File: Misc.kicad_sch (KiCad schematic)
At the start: 14 parts, among them J501 Conn_01x04, U500 TJA1051T-3

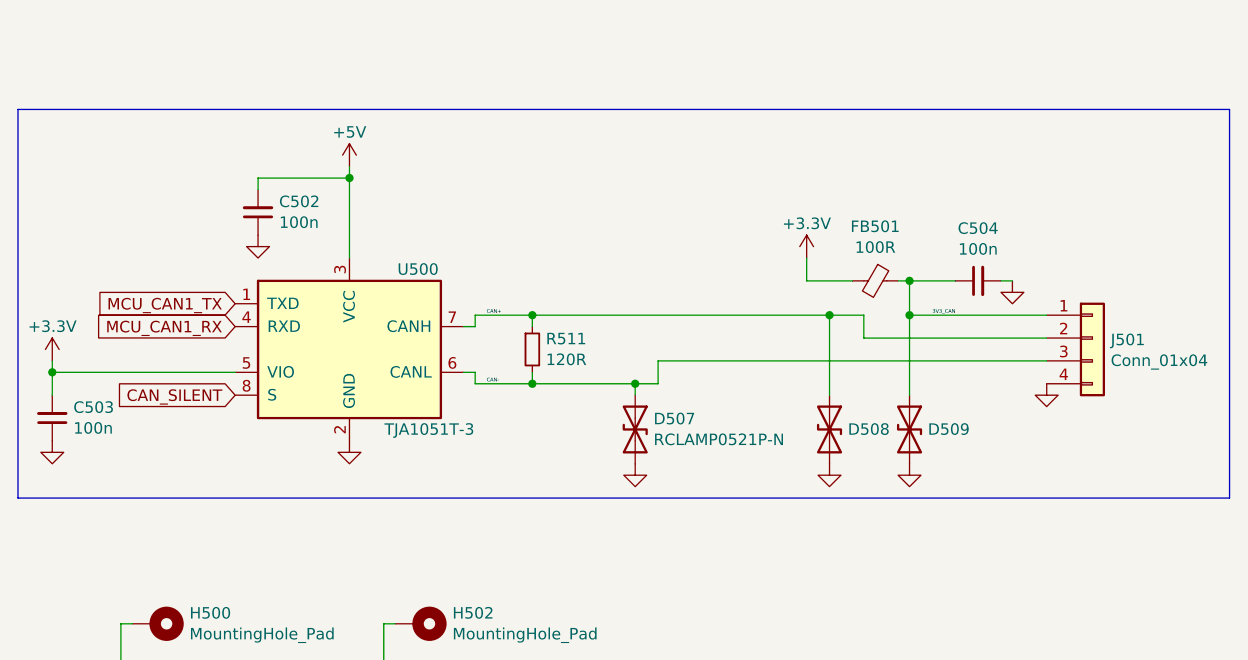
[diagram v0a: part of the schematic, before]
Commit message: replaced CAN transceiver, introduced new IMU
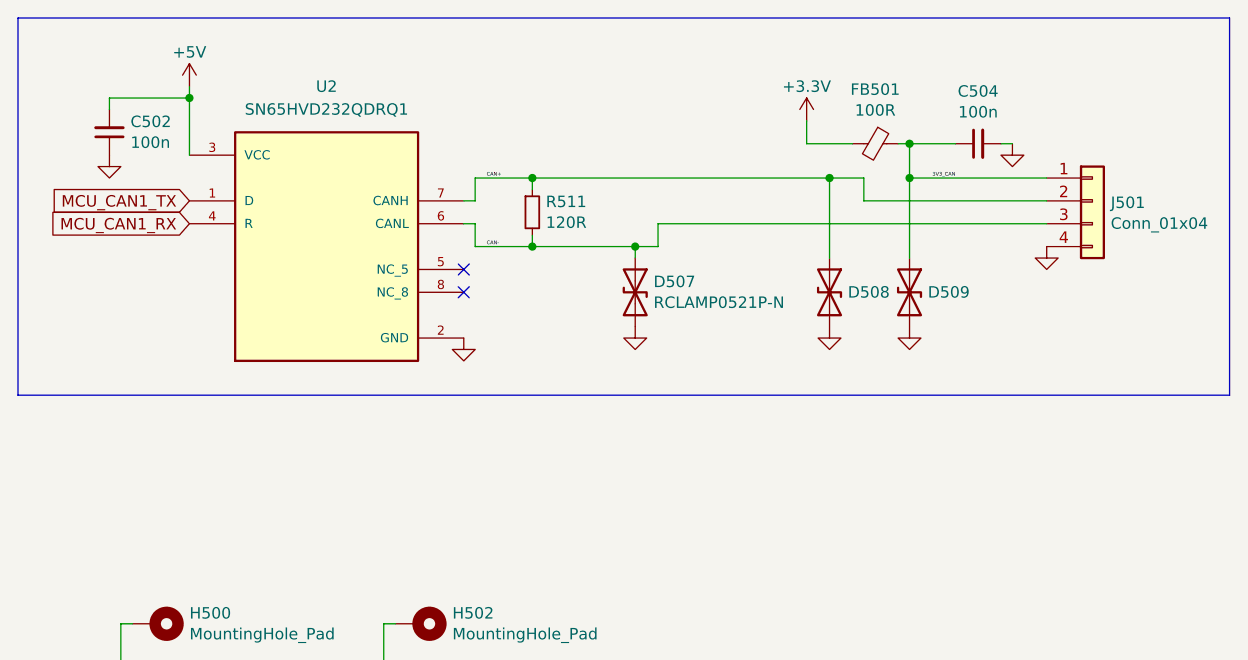
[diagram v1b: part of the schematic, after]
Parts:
- removed C503: 100n, Capacitor_SMD:C_0402_1005Metric, symbol Device:C_Small
- removed U500: TJA1051T-3, Package_SO:SOIC-8_3.9x4.9mm_P1.27mm, symbol Interface_CAN_LIN:TJA1051T-3
- added U2: SN65HVD232QDRQ1, SnapEDA Library:SOIC127P599X175-8N, symbol SN65HVD232QDRQ1:SN65HVD232QDRQ1
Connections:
- net +5V: now also U2.3 (VCC)
- net CAN+: now also U2.7 (CANH)
- net CAN-: now also U2.6 (CANL)
- net GND: now also U2.2 (GND)
- net MCU_CAN1_RX: now also U2.4 (R)
- net MCU_CAN1_TX: now also U2.1 (D)
- no-connect marks 0 -> 2
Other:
- moved on the sheet: C502, C504, D507, D508, D509, FB501, J501, R511

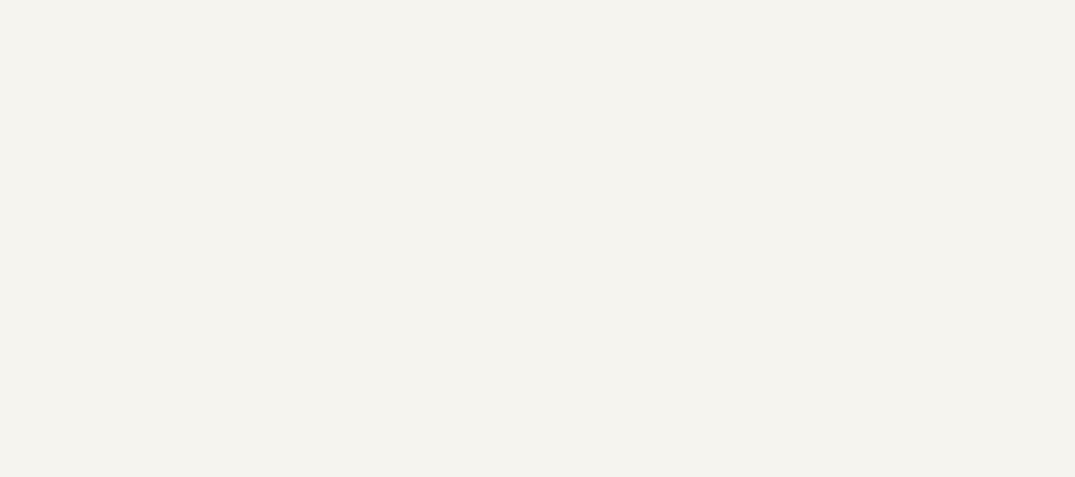
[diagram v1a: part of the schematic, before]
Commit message: added cubeide workspace
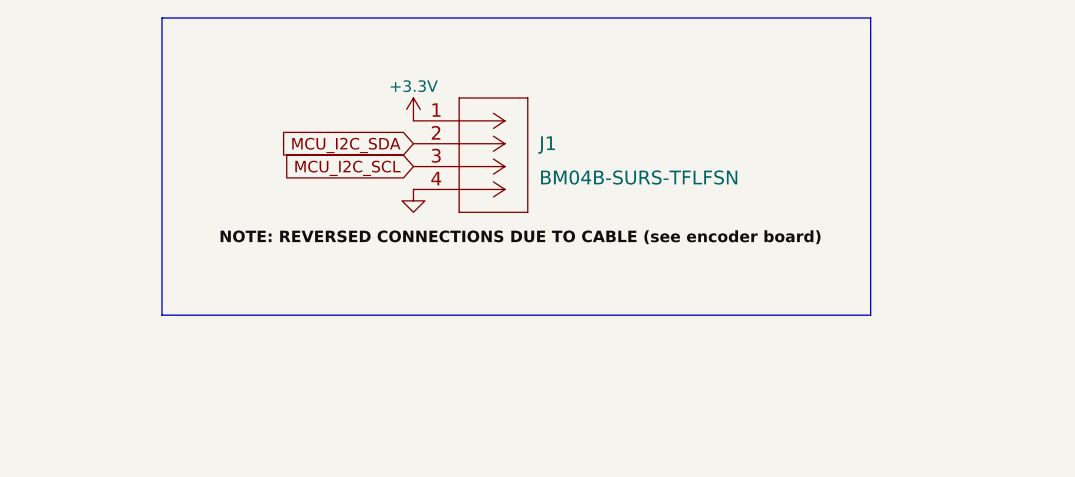
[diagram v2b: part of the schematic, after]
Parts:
- added J1: BM04B-SURS-TFLFSN, CONN_BM04B-SURS-TF_JST, symbol BM04B:BM04B-SURS-TFLFSN
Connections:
- net +3V3: now also J1.1
- net GND: now also J1.4
- new net MCU_I2C_SCL: J1.3
- new net MCU_I2C_SDA: J1.2
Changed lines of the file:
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@@
+    (stroke (width 0) (type default) (color 0 0 0 0))
+  )
+  (polyline (pts (xy 109.22 72.39) (xy 187.96 72.39))
     (stroke (width 0) (type default) (color 0 0 0 0))
   )
@@
     (stroke (width 0) (type default) (color 0 0 0 0))
   )
+  (polyline (pts (xy 109.22 39.37) (xy 109.22 72.39))
+    (stroke (width 0) (type default) (color 0 0 0 0))
+  )
+  (polyline (pts (xy 187.96 72.39) (xy 187.96 39.37))
+    (stroke (width 0) (type default) (color 0 0 0 0))
+  )
   (wire (pts (xy 156.21 127) (xy 156.21 129.54))
     (stroke (width 0) (type default) (color 0 0 0 0))
@@
     (stroke (width 0) (type default) (color 0 0 0 0))
   )
+  (polyline (pts (xy 187.96 39.37) (xy 109.22 39.37))
+    (stroke (width 0) (type default) (color 0 0 0 0))
+  )
   (wire (pts (xy 184.15 121.92) (xy 199.39 121.92))
     (stroke (width 0) (type default) (color 0 0 0 0))
@@
   (wire (pts (xy 104.14 113.03) (xy 95.25 113.03))
     (stroke (width 0) (type default) (color 0 0 0 0))
+  )
+  (label "NOTE: REVERSED CONNECTIONS DUE TO CABLE (see encoder board)"
+    (at 115.57 64.77 0)
+    (effects (font (size 1.27 1.27) (thickness 0.254) bold) (justify left bottom))
   )
   (label "CAN+" (at 137.16 121.92 0)
@@
     )
   )
+  (global_label "MCU_I2C_SCL" (shape input) (at 137.16 55.88 180) (fields_autoplaced)
+    (effects (font (size 1.27 1.27)) (justify right))
+    (property "Intersheet References" "${INTERSHEET_REFS}" (id 0) (at 122.2568 55.8006 0)
+      (effects (font (size 1.27 1.27)) (justify right) hide)
+    )
+  )
   (global_label "MCU_CAN1_TX" (shape input) (at 104.14 124.46 180) (fields_autoplaced)
     (effects (font (size 1.27 1.27)) (justify right))
@@
     )
   )
+  (global_label "MCU_I2C_SDA" (shape input) (at 137.16 53.34 180) (fields_autoplaced)
+    (effects (font (size 1.27 1.27)) (justify right))
+    (property "Intersheet References" "${INTERSHEET_REFS}" (id 0) (at 122.1963 53.2606 0)
+      (effects (font (size 1.27 1.27)) (justify right) hide)
+    )
+  )
   (symbol (lib_id "power:GND") (at 134.62 139.7 0) (unit 1)
     (in_bom yes) (on_board yes)
@@
     (pin "1")
     (pin "2")
+  )
+  (symbol (lib_id "BluePhil-rescue:+3.3V-power") (at 137.16 50.8 0) (unit 1)
+    (in_bom yes) (on_board yes)
+    (property "Reference" "#PWR032" (id 0) (at 137.16 54.61 0)
+      (effects (font (size 1.27 1.27)) hide)
+    )
+    (property "Value" "+3.3V" (id 1) (at 137.16 46.99 0))
+    (property "Footprint" "" (id 2) (at 137.16 50.8 0)
+      (effects (font (size 1.27 1.27)) hide)
+    )
+    (property "Datasheet" "" (id 3) (at 137.16 50.8 0)
+      (effects (font (size 1.27 1.27)) hide)
+    )
+    (pin "1")
   )
   (symbol (lib_id "SN65HVD232QDRQ1:SN65HVD232QDRQ1") (at 119.38 129.54 0) (unit 1)
@@
     (pin "8")
   )
+  (symbol (lib_id "BM04B:BM04B-SURS-TFLFSN") (at 137.16 50.8 0) (unit 1)
+    (in_bom yes) (on_board yes) (fields_autoplaced)
+    (property "Reference" "J1" (id 0) (at 151.13 53.34 0)
+      (effects (font (size 1.524 1.524)) (justify left))
+    )
+    (property "Value" "BM04B-SURS-TFLFSN" (id 1) (at 151.13 57.15 0)
+      (effects (font (size 1.524 1.524)) (justify left))
+    )
+    (property "Footprint" "CONN_BM04B-SURS-TF_JST" (id 2) (at 147.32 57.404 0)
+      (effects (font (size 1.524 1.524)) hide)
+    )
+    (property "Datasheet" "" (id 3) (at 137.16 50.8 0)
+      (effects (font (size 1.524 1.524)))
+    )
+    (pin "1")
+    (pin "2")
+    (pin "3")
+    (pin "4")
+  )
+  (symbol (lib_id "power:GND") (at 137.16 58.42 0) (unit 1)
+    (in_bom yes) (on_board yes)
+    (property "Reference" "#PWR033" (id 0) (at 137.16 64.77 0)
+      (effects (font (size 1.27 1.27)) hide)
+    )
+    (property "Value" "GND" (id 1) (at 137.16 62.23 0)
+      (effects (font (size 1.27 1.27)) hide)
+    )
+    (property "Footprint" "" (id 2) (at 137.16 58.42 0)
+      (effects (font (size 1.27 1.27)) hide)
+    )
+    (property "Datasheet" "" (id 3) (at 137.16 58.42 0)
+      (effects (font (size 1.27 1.27)) hide)
+    )
+    (pin "1")
+  )
 )

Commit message: more changes!
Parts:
- J1: footprint CONN_BM04B-SURS-TF_JST -> BM04B:BM04B-SURS-TFLFSN
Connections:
- net +5V is gone; now on net +3V3: C502.2, U2.3 (VCC)
- net MCU_I2C_SCL renamed MCU_I2C1_SCL
- net MCU_I2C_SDA renamed MCU_I2C1_SDA
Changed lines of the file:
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@@
     )
   )
-  (global_label "MCU_I2C_SCL" (shape input) (at 137.16 55.88 180) (fields_autoplaced)
+  (global_label "MCU_I2C1_SCL" (shape input) (at 137.16 55.88 180) (fields_autoplaced)
     (effects (font (size 1.27 1.27)) (justify right))
-    (property "Intersheet References" "${INTERSHEET_REFS}" (id 0) (at 122.2568 55.8006 0)
+    (property "Intersheet References" "${INTERSHEET_REFS}" (id 0) (at 121.0472 55.8006 0)
       (effects (font (size 1.27 1.27)) (justify right) hide)
     )
@@
     )
   )
-  (global_label "MCU_I2C_SDA" (shape input) (at 137.16 53.34 180) (fields_autoplaced)
+  (global_label "MCU_I2C1_SDA" (shape input) (at 137.16 53.34 180) (fields_autoplaced)
     (effects (font (size 1.27 1.27)) (justify right))
-    (property "Intersheet References" "${INTERSHEET_REFS}" (id 0) (at 122.1963 53.2606 0)
+    (property "Intersheet References" "${INTERSHEET_REFS}" (id 0) (at 120.9868 53.2606 0)
       (effects (font (size 1.27 1.27)) (justify right) hide)
     )
@@
     (pin "1")
     (pin "2")
-  )
-  (symbol (lib_id "power:+5V") (at 104.14 111.76 0) (unit 1)
-    (in_bom yes) (on_board yes)
-    (property "Reference" "#PWR051" (id 0) (at 104.14 115.57 0)
-      (effects (font (size 1.27 1.27)) hide)
-    )
-    (property "Value" "+5V" (id 1) (at 104.14 107.95 0))
-    (property "Footprint" "" (id 2) (at 104.14 111.76 0)
-      (effects (font (size 1.27 1.27)) hide)
-    )
-    (property "Datasheet" "" (id 3) (at 104.14 111.76 0)
-      (effects (font (size 1.27 1.27)) hide)
-    )
-    (pin "1")
   )
   (symbol (lib_id "Mechanical:MountingHole_Pad") (at 100.33 177.8 270) (unit 1)
@@
       (effects (font (size 1.524 1.524)) (justify left))
     )
-    (property "Footprint" "CONN_BM04B-SURS-TF_JST" (id 2) (at 147.32 57.404 0)
+    (property "Footprint" "BM04B:BM04B-SURS-TFLFSN" (id 2) (at 147.32 57.404 0)
       (effects (font (size 1.524 1.524)) hide)
     )
@@
     (pin "4")
   )
+  (symbol (lib_id "BluePhil-rescue:+3.3V-power") (at 104.14 111.76 0) (unit 1)
+    (in_bom yes) (on_board yes)
+    (property "Reference" "#PWR?" (id 0) (at 104.14 115.57 0)
+      (effects (font (size 1.27 1.27)) hide)
+    )
+    (property "Value" "+3.3V" (id 1) (at 104.14 107.95 0))
+    (property "Footprint" "" (id 2) (at 104.14 111.76 0)
+      (effects (font (size 1.27 1.27)) hide)
+    )
+    (property "Datasheet" "" (id 3) (at 104.14 111.76 0)
+      (effects (font (size 1.27 1.27)) hide)
+    )
+    (pin "1")
+  )
   (symbol (lib_id "power:GND") (at 137.16 58.42 0) (unit 1)

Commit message: more progress
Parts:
- added J2: Conn_02x08_Top_Bottom, Connector_PinSocket_2.54mm:PinSocket_2x08_P2.54mm_Vertical, symbol Connector_Generic:Conn_02x08_Top_Bottom
- added J3, J4: Conn_01x04, Connector_PinSocket_2.54mm:PinSocket_1x04_P2.54mm_Vertical, symbol Connector_Generic:Conn_01x04
- added J5: Conn_01x05, Connector_PinSocket_2.54mm:PinSocket_1x05_P2.54mm_Vertical, symbol Connector_Generic:Conn_01x05
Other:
- moved on the sheet: C502, C504, D507, D508, D509, FB501, H500, H501, H502, H503, J1, J501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
